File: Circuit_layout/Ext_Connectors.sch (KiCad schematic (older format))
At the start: 17 parts, among them CON1 AVR-JTAG-10, J1 CONN_01X03, J10 CONN_01X02, J11 CONN_8, J2 CONN_01X03, J3 CONN_01X02, J4 CONN_01X04, J5 RJ12, J6 CONN_01X02, J7 CONN_01X06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

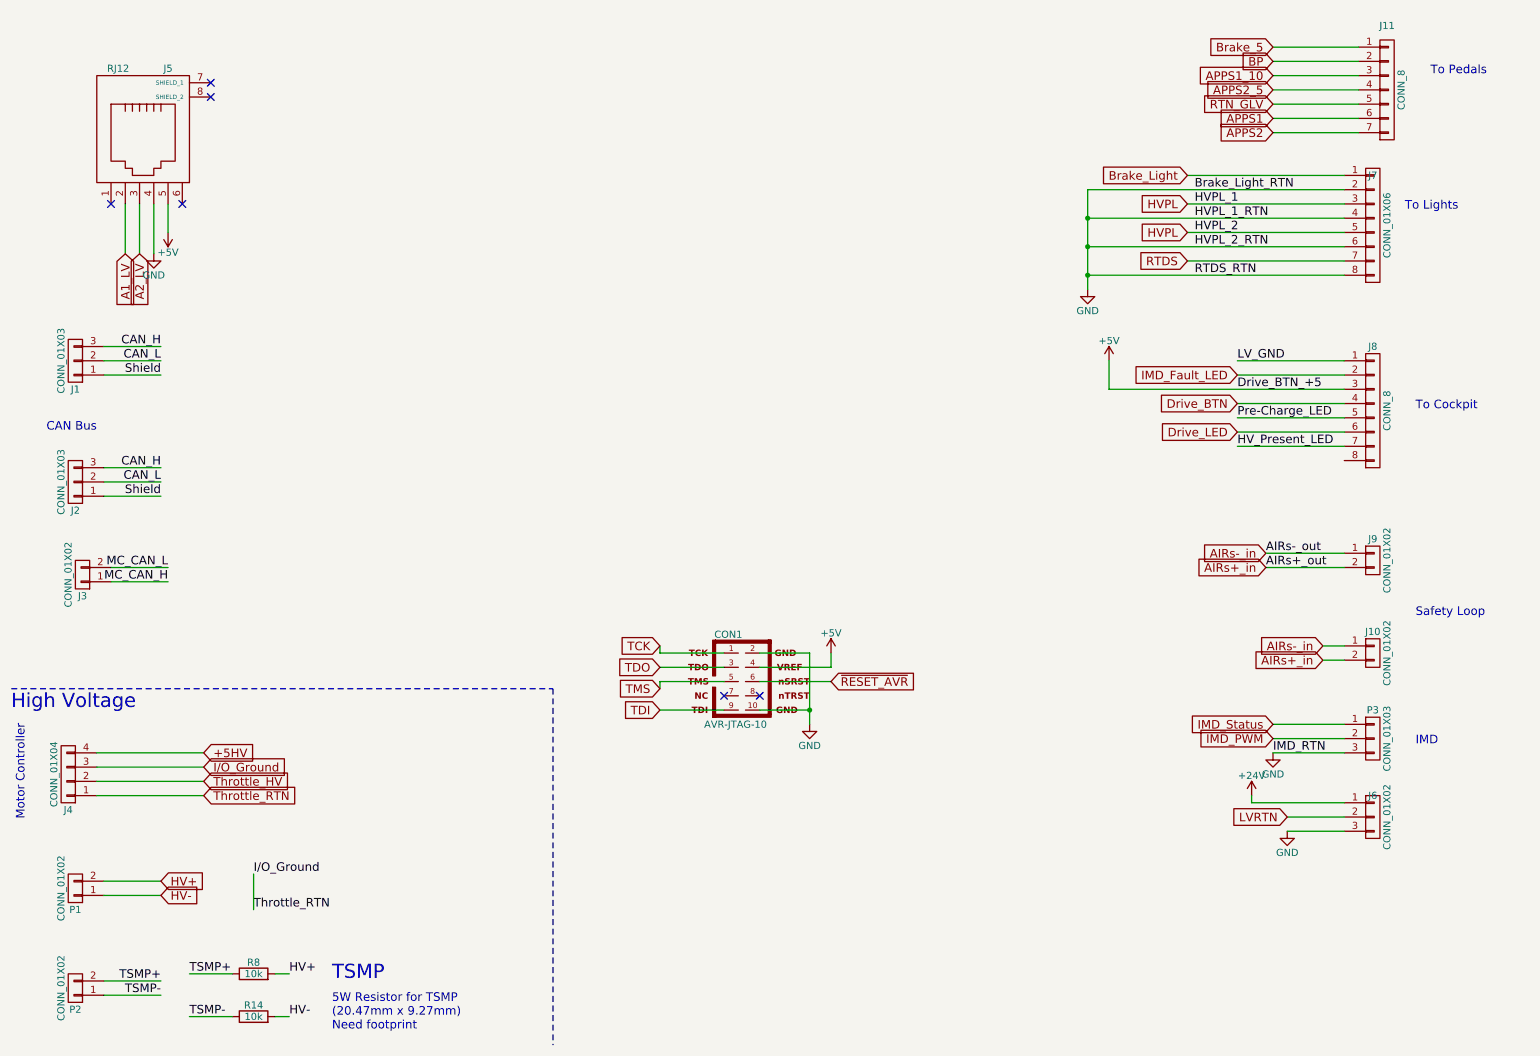
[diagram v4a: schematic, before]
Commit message: eliminated warnings, need to clean things up + add footprints/datasheets
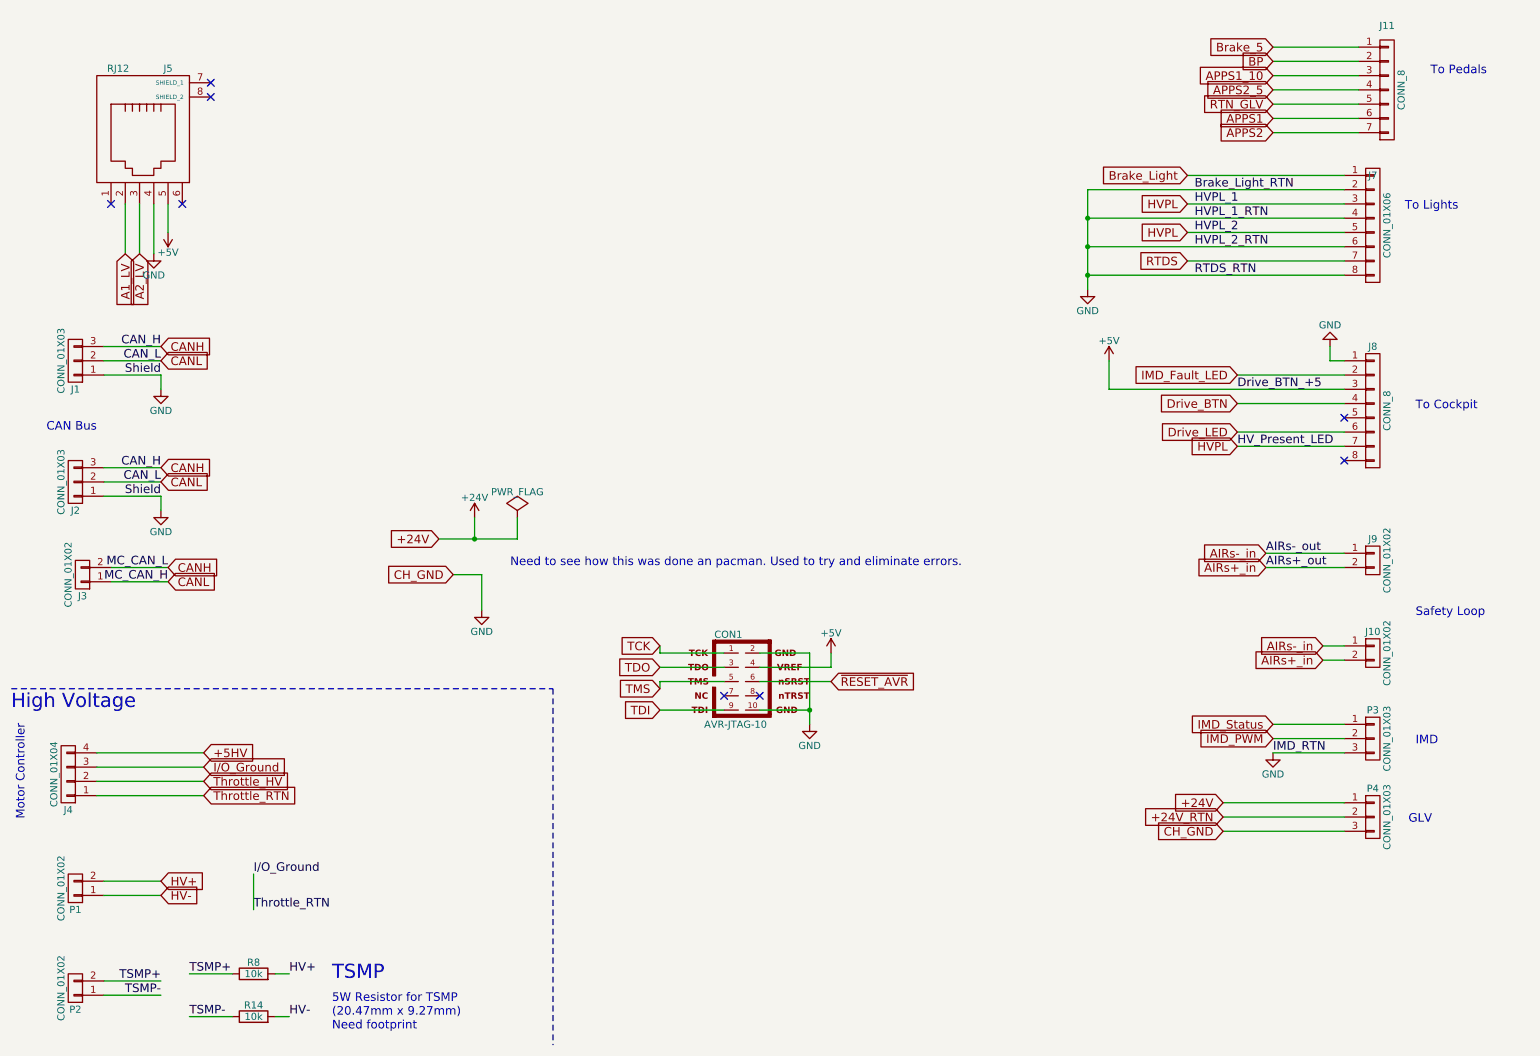
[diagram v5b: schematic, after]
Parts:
- removed J6: CONN_01X02, symbol CONN_01X03
- added P4: CONN_01X03, symbol CONN_01X03
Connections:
- net HV_Present_LED is gone; now on net HVPL: J8.7 (P7)
- net LV_GND is gone; now on net GND: J8.1 (P1)
- net MC_CAN_H is gone; now on net CANL: J3.1 (P1)
- net MC_CAN_L is gone; now on net CANH: J3.2 (P2)
- net Shield is gone; now on net GND: J1.1 (P1), J2.1 (P1)
- net +24V: now also P4.1 (P1)
- net GND: now also P4.3 (P3)
- net CAN_H renamed CANH
- net CAN_L renamed CANL
- net Pre-Charge_LED: no longer names the net of J8.5 (P5)
- new net +24V_RTN: P4.2 (P2)
- no-connect marks 6 -> 8
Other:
- note added: "GLV"
- note added: "Need to see how this was done an pacman. Used to try and eliminate errors.\n"
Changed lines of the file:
@@
 Text Notes 10350 3350 0    60   ~ 0
 To Cockpit
-Text Label 9100 3400 0    60   ~ 0
-Pre-Charge_LED
 Text Label 9100 3600 0    60   ~ 0
 HV_Present_LED
@@
 Text Notes 10650 1950 2    60   ~ 0
 To Lights
-$Comp
-L CONN_01X03 J6
-U 1 1 58A769F6
-P 10050 6200
-F 0 "J6" H 10050 6350 50  0000 C CNN
-F 1 "CONN_01X02" V 10150 6200 50  0000 C CNN
-F 2 "" H 10050 6200 50  0000 C CNN
-F 3 "" H 10050 6200 50  0000 C CNN
-F 4 "W1" H 10050 6200 60  0001 C CNN "Wire Number"
-	1    10050 6200
-	1    0    0    -1
-$EndComp
 $Comp
 L CONN_01X02 J3
@@
 	1    0    0    -1
 $EndComp
-Text GLabel 9450 6200 0    60   Input ~ 0
-LVRTN
+Text GLabel 9000 6200 0    60   Input ~ 0
++24V_RTN
 $Comp
 L +24V #PWR018
 U 1 1 58AF1C5B
-P 9200 6050
-F 0 "#PWR018" H 9200 5900 50  0001 C CNN
-F 1 "+24V" H 9200 6190 50  0000 C CNN
-F 2 "" H 9200 6050 50  0000 C CNN
-F 3 "" H 9200 6050 50  0000 C CNN
-	1    9200 6050
+P 3750 4100
+F 0 "#PWR018" H 3750 3950 50  0001 C CNN
+F 1 "+24V" H 3750 4240 50  0000 C CNN
+F 2 "" H 3750 4100 50  0000 C CNN
+F 3 "" H 3750 4100 50  0000 C CNN
+	1    3750 4100
 	1    0    0    -1
 $EndComp
@@
 5W Resistor for TSMP\n(20.47mm x 9.27mm)\nNeed footprint
 Wire Wire Line
-	1200 4450 1600 4450
-Wire Wire Line
-	1200 4550 1600 4550
-Wire Wire Line
-	9850 6200 9450 6200
-Wire Wire Line
-	9200 6100 9850 6100
-Wire Wire Line
 	1100 5850 1850 5850
 Wire Wire Line
@@
 	9850 3500 9100 3500
 Wire Wire Line
-	9100 3400 9850 3400
-Wire Wire Line
 	9100 3300 9850 3300
 Wire Wire Line
@@
 	9850 3100 9100 3100
 Wire Wire Line
-	9850 3000 9100 3000
-Wire Wire Line
 	8750 2100 9850 2100
 Wire Wire Line
@@
 Wire Wire Line
 	9950 800  9350 800
-Wire Wire Line
-	1150 3950 1550 3950
-Wire Wire Line
-	1150 3850 1550 3850
-Wire Wire Line
-	1150 3750 1550 3750
-Wire Wire Line
-	1150 3100 1550 3100
-Wire Wire Line
-	1150 3000 1550 3000
-Wire Wire Line
-	1150 2900 1550 2900
 Wire Wire Line
 	1150 6750 1550 6750
@@
 Wire Wire Line
 	5050 5050 5050 5000
-Wire Wire Line
-	9850 6300 9450 6300
 Wire Wire Line
 	1100 5750 1850 5750
@@
 TSMP-
 $Comp
-L GND #PWR021
-U 1 1 58B6646E
-P 9450 6300
-F 0 "#PWR021" H 9450 6050 50  0001 C CNN
-F 1 "GND" H 9450 6150 50  0000 C CNN
-F 2 "" H 9450 6300 50  0000 C CNN
-F 3 "" H 9450 6300 50  0000 C CNN
-	1    9450 6300
-	1    0    0    -1
-$EndComp
-$Comp
 L CONN_01X03 P3
 U 1 1 58B7F8E6
@@
 IMD
 Wire Wire Line
-	9200 6100 9200 6050
-Wire Wire Line
 	9350 5750 9850 5750
 Wire Wire Line
@@
 	8050 2000 9850 2000
 $Comp
-L +5V #PWR022
+L +5V #PWR021
 U 1 1 58BB5596
 P 1600 2100
-F 0 "#PWR022" H 1600 1950 50  0001 C CNN
+F 0 "#PWR021" H 1600 1950 50  0001 C CNN
 F 1 "+5V" H 1600 2240 50  0000 C CNN
 F 2 "" H 1600 2100 50  0000 C CNN
@@
 $EndComp
 $Comp
-L GND #PWR023
+L GND #PWR022
 U 1 1 58BB55DD
 P 1500 2250
-F 0 "#PWR023" H 1500 2000 50  0001 C CNN
+F 0 "#PWR022" H 1500 2000 50  0001 C CNN
 F 1 "GND" H 1500 2100 50  0000 C CNN
 F 2 "" H 1500 2250 50  0000 C CNN
@@
 A1_LV
 $Comp
-L GND #PWR024
+L GND #PWR023
 U 1 1 58BB7C87
 P 9350 5750
-F 0 "#PWR024" H 9350 5500 50  0001 C CNN
+F 0 "#PWR023" H 9350 5500 50  0001 C CNN
 F 1 "GND" H 9350 5600 50  0000 C CNN
 F 2 "" H 9350 5750 50  0000 C CNN
@@
 Wire Wire Line
 	8200 3200 8200 3000
-Text Label 9100 3000 0    60   ~ 0
-LV_GND
+$Comp
+L CONN_01X03 P4
+U 1 1 58B75CBA
+P 10050 6200
+F 0 "P4" H 10050 6400 50  0000 C CNN
+F 1 "CONN_01X03" V 10150 6200 50  0000 C CNN
+F 2 "" H 10050 6200 50  0000 C CNN
+F 3 "" H 10050 6200 50  0000 C CNN
+	1    10050 6200
+	1    0    0    -1
+$EndComp
+Text GLabel 9000 6300 0    60   Input ~ 0
+CH_GND
+NoConn ~ 9850 3700
+$Comp
+L GND #PWR024
+U 1 1 58B7A0E8
+P 9750 2900
+F 0 "#PWR024" H 9750 2650 50  0001 C CNN
+F 1 "GND" H 9750 2750 50  0000 C CNN
+F 2 "" H 9750 2900 50  0000 C CNN
+F 3 "" H 9750 2900 50  0000 C CNN
+	1    9750 2900
+	-1   0    0    1
+$EndComp
+Text GLabel 3600 4500 0    60   Input ~ 0
+CH_GND
+$Comp
+L GND #PWR025
+U 1 1 58B888D9
+P 3800 4750
+F 0 "#PWR025" H 3800 4500 50  0001 C CNN
+F 1 "GND" H 3800 4600 50  0000 C CNN
+F 2 "" H 3800 4750 50  0000 C CNN
+F 3 "" H 3800 4750 50  0000 C CNN
+	1    3800 4750
+	1    0    0    -1
+$EndComp
+Wire Wire Line
+	3600 4500 3800 4500
+Wire Wire Line
+	3800 4500 3800 4750
+Text GLabel 9000 6100 0    60   Input ~ 0
++24V
+Text GLabel 3500 4250 0    60   Input ~ 0
++24V
+Wire Wire Line
+	3500 4250 4050 4250
+Wire Wire Line
+	3750 4250 3750 4100
+$Comp
+L PWR_FLAG #FLG026
+U 1 1 58B89230
+P 4050 4100
+F 0 "#FLG026" H 4050 4195 50  0001 C CNN
+F 1 "PWR_FLAG" H 4050 4280 50  0000 C CNN
+F 2 "" H 4050 4100 50  0000 C CNN
+F 3 "" H 4050 4100 50  0000 C CNN
+	1    4050 4100
+	1    0    0    -1
+$EndComp
+Wire Wire Line
+	4050 4250 4050 4100
+Connection ~ 3750 4250
+Wire Wire Line
+	9000 6300 9850 6300
+Wire Wire Line
+	9000 6100 9850 6100
+NoConn ~ 9850 3400
+Text GLabel 9100 3600 0    60   Input ~ 0
+HVPL
+Wire Wire Line
+	9750 2900 9750 3000
+Wire Wire Line
+	9750 3000 9850 3000
+Text Notes 4000 4450 0    60   ~ 0
+Need to see how this was done an pacman. Used to try and eliminate errors.\n
+Text GLabel 1550 2900 2    60   Input ~ 0
+CANH
+Text GLabel 1550 3000 2    60   Input ~ 0
+CANL
+Text GLabel 1550 3750 2    60   Input ~ 0
+CANH
+Text GLabel 1550 3850 2    60   Input ~ 0
+CANL
+Text GLabel 1600 4450 2    60   Input ~ 0
+CANH
+Text GLabel 1600 4550 2    60   Input ~ 0
+CANL
+Wire Wire Line
+	1200 4550 1600 4550
+Wire Wire Line
+	1600 4450 1200 4450
+Wire Wire Line
+	1150 3850 1550 3850
+Wire Wire Line
+	1150 3750 1550 3750
+Wire Wire Line
+	1150 3000 1550 3000
+Wire Wire Line
+	1150 2900 1550 2900
+Wire Wire Line
+	1150 3100 1550 3100
+Wire Wire Line
+	1150 3950 1550 3950
+$Comp
+L GND #PWR027
+U 1 1 58B8F80F
+P 1550 4050
+F 0 "#PWR027" H 1550 3800 50  0001 C CNN
+F 1 "GND" H 1550 3900 50  0000 C CNN
+F 2 "" H 1550 4050 50  0000 C CNN
+F 3 "" H 1550 4050 50  0000 C CNN
+	1    1550 4050
+	1    0    0    -1
+$EndComp
+$Comp
+L GND #PWR028
+U 1 1 58B8F891
+P 1550 3200
+F 0 "#PWR028" H 1550 2950 50  0001 C CNN
+F 1 "GND" H 1550 3050 50  0000 C CNN
+F 2 "" H 1550 3200 50  0000 C CNN
+F 3 "" H 1550 3200 50  0000 C CNN
+	1    1550 3200
+	1    0    0    -1
+$EndComp
+Wire Wire Line
+	1550 3100 1550 3200
+Wire Wire Line
+	1550 3950 1550 4050
+Wire Wire Line
+	9000 6200 9850 6200
+Text Notes 10300 6250 0    60   ~ 0
+GLV
 $EndSCHEMATC

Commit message: Working on neatining up schematic and working on top level diagram
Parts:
- removed J1, J2: CONN_01X03, symbol CONN_01X03
- removed J9: CONN_01X02, symbol CONN_01X02
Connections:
- net AIRs+_in renamed AIRs-
- net AIRs-_in renamed AIRs+
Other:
- note added: "AIRs"
- note removed: "Safety Loop"
- moved on the sheet: J10, J3, P3, P4

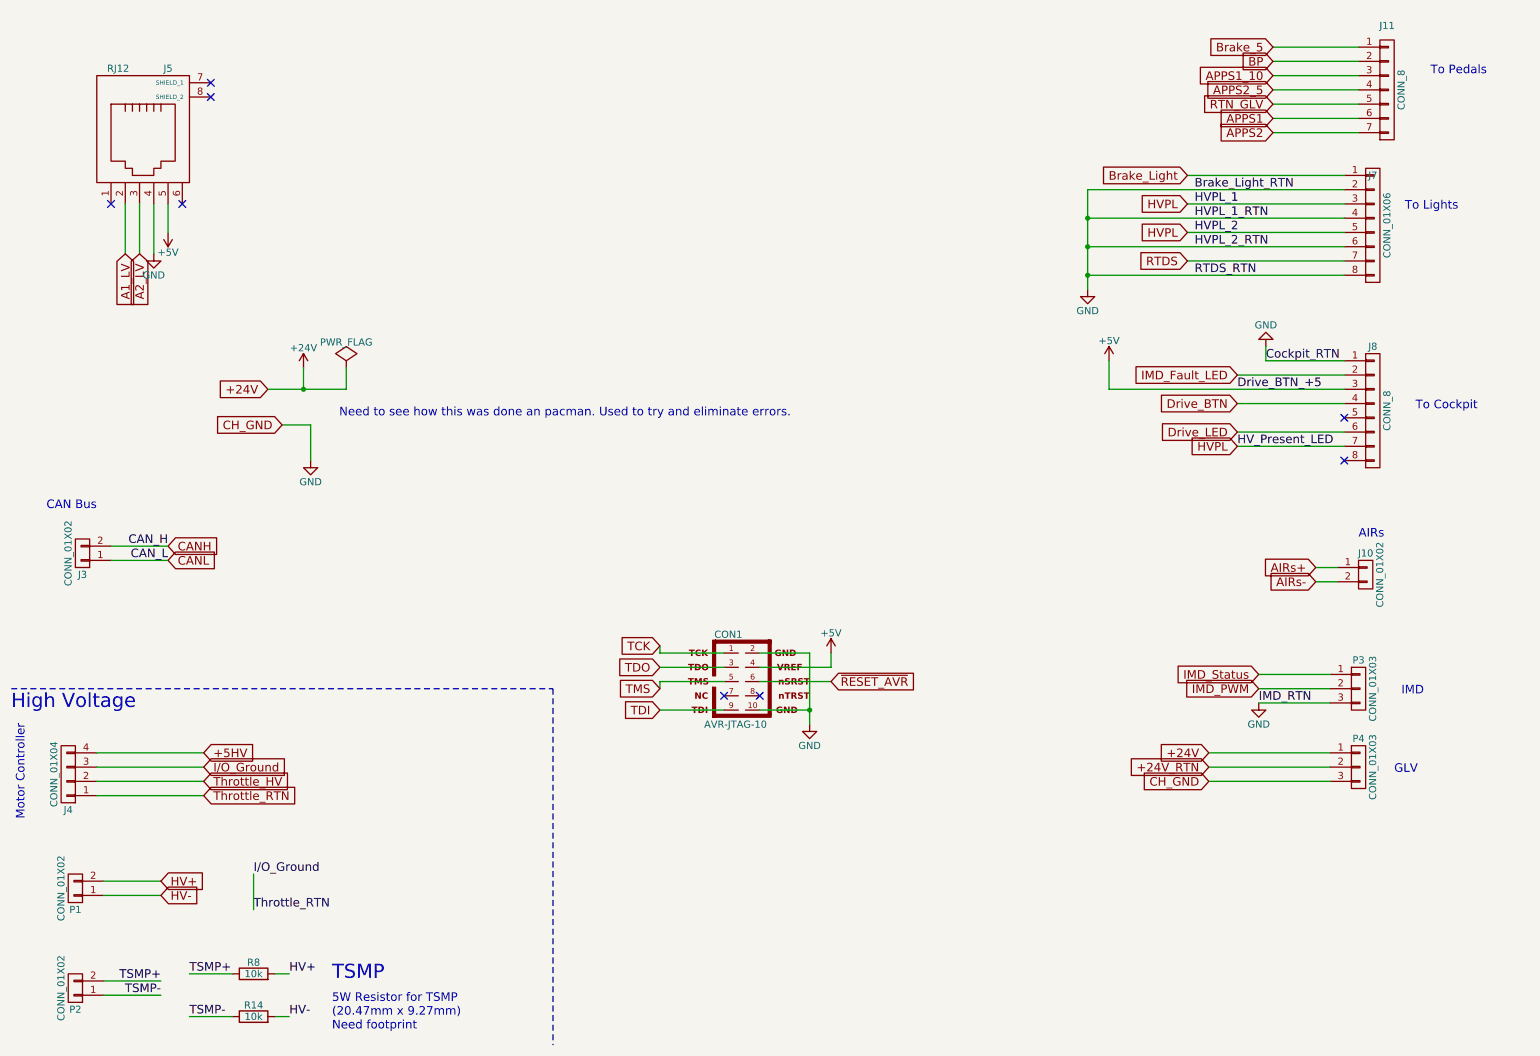
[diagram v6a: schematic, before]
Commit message: cleaned up sch, added bypass pass. no net warnings
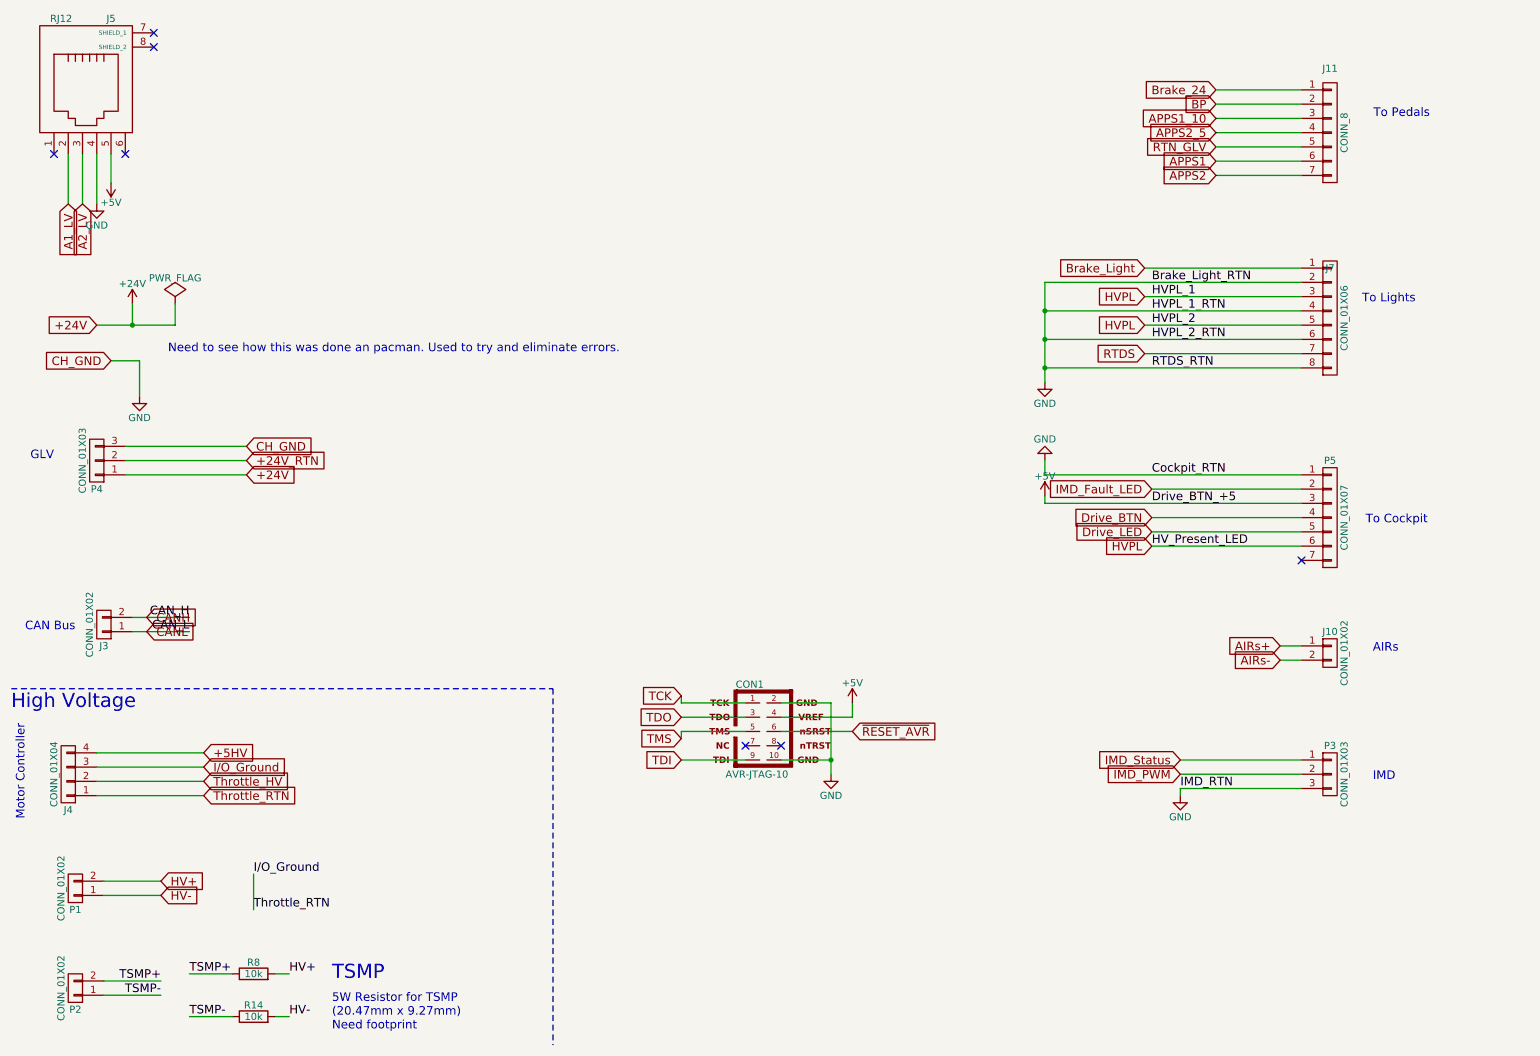
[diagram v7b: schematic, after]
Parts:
- removed J8: CONN_8, symbol CONN_8
- added P5: CONN_01X07, symbol CONN_01X07
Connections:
- net +5V: now also P5.3 (P3)
- net Drive_BTN: now also P5.4 (P4)
- net Drive_LED: now also P5.5 (P5)
- net GND: now also P5.1 (P1)
- net HVPL: now also P5.6 (P6)
- net IMD_Fault_LED: now also P5.2 (P2)
- net Brake_5 renamed Brake_24
- no-connect marks 8 -> 7
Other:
- moved on the sheet: CON1, J10, J11, J3, J5, J7, P3, P4
